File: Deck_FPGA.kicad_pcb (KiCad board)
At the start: 4 copper layers, 41 x 30 mm, 72 parts, among them J1 Left side, J2 Right Side, J3 Conn_01x06, U1 XC7A100T-CSG324, U2 TPS65023BRSBT, U3 S25FL128SAGNFI000, U4 LM3880, X1 ASE-100MHz

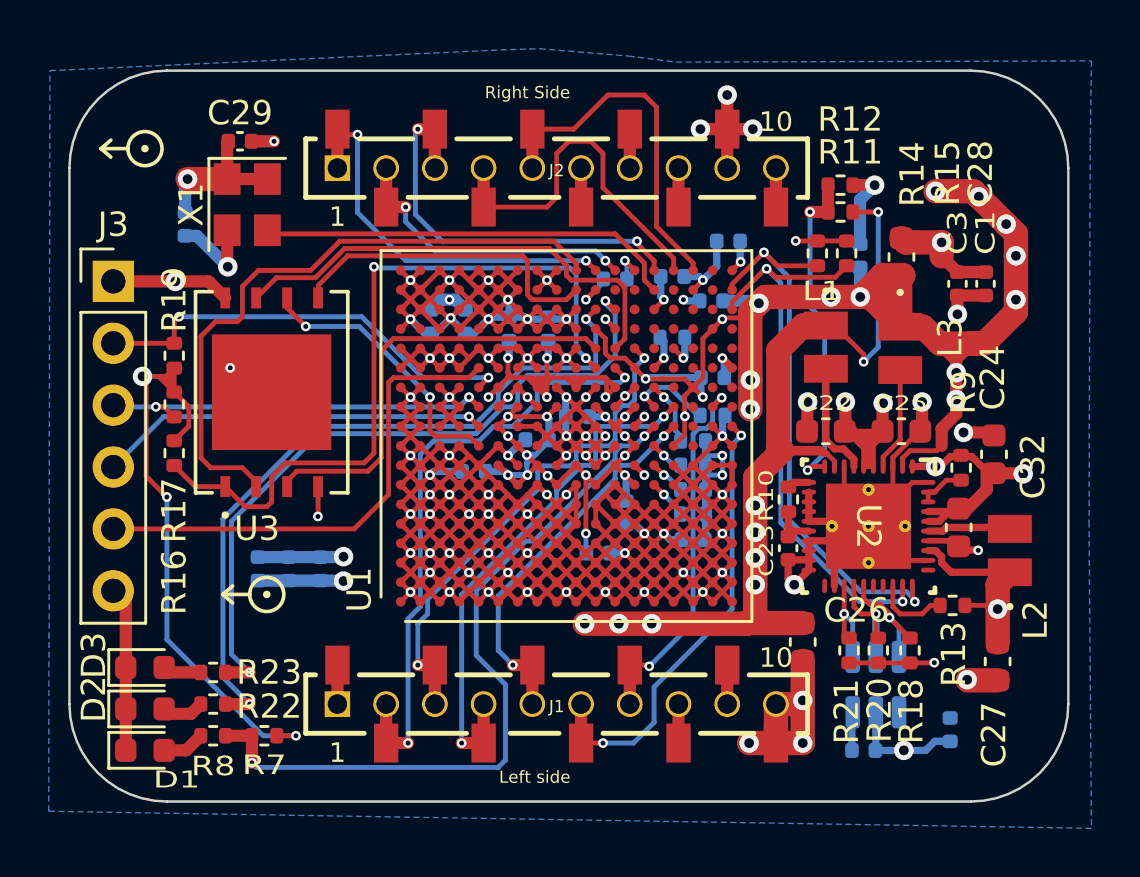
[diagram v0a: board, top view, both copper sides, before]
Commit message: added PowerIC filtering resistor and pull up for SPI Flash SIO2/SIO3
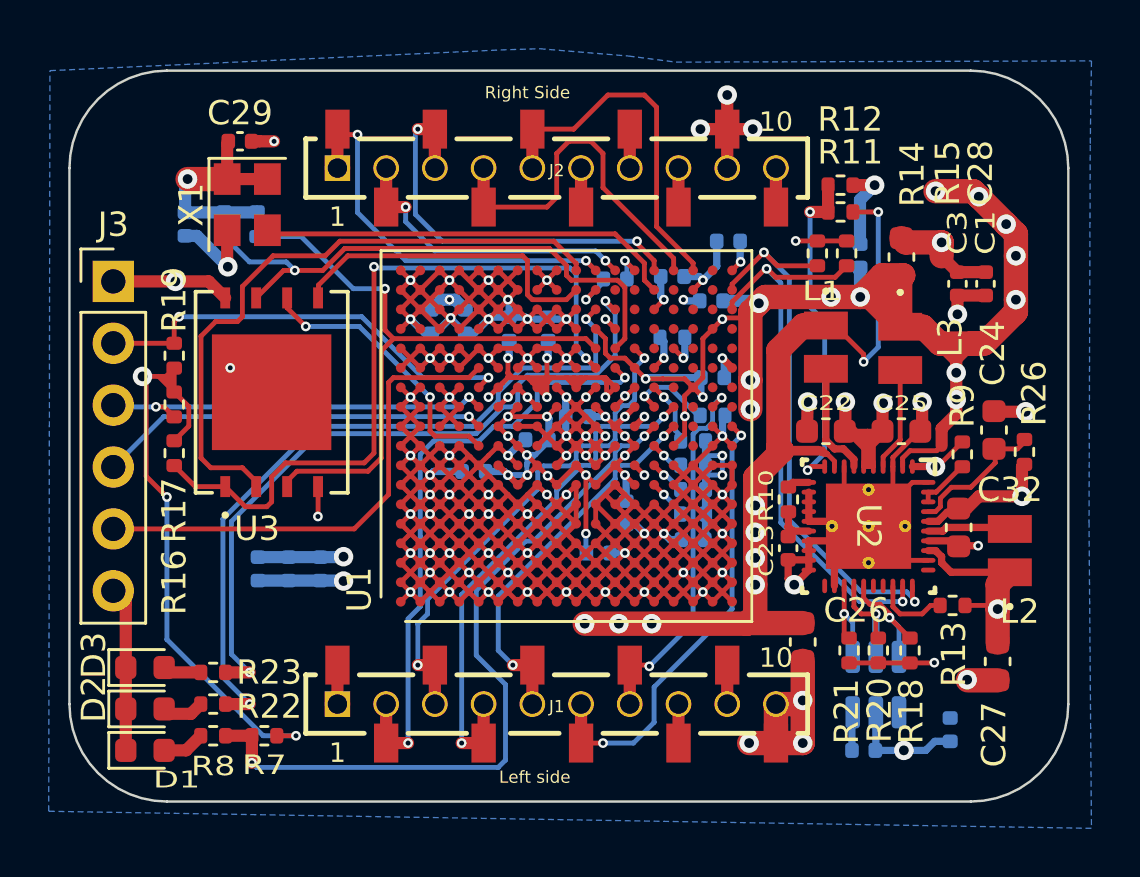
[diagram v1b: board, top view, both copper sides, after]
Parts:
- removed REF** (x2): arrow, ul:arrow
- added R24: 4k7, Resistor_SMD:R_0402_1005Metric, B.Cu at (87.7, 102.3)
- added R25: 4k7, Resistor_SMD:R_0402_1005Metric, B.Cu at (86.3, 102.3)
- added R26: 10R, Resistor_SMD:R_0402_1005Metric, F.Cu at (119.2, 111.7)
- C22, C25, C32: value 10u -> 22u
- R14, R15: value 100k -> 4k7
- moved C24 1.00 mm to (118.0, 110.8)
- moved R9 0.55 mm to (116.7, 111.8)
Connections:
- C24 pad 1: VBUS -> /VCC
- U2 pad 37: VBUS -> /VCC
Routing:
- net /SIO2: track 18.1 -> 26.4 mm, vias 0 -> 1
- net /VCC: track 0.00 -> 5.82 mm
- net /SIO3: track 19.5 -> 23.0 mm, vias 0 -> 1
- net +3V3: track 110.8 -> 113.8 mm
- net VBUS: track 33.4 -> 31.0 mm

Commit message: fixed caps, jlc references
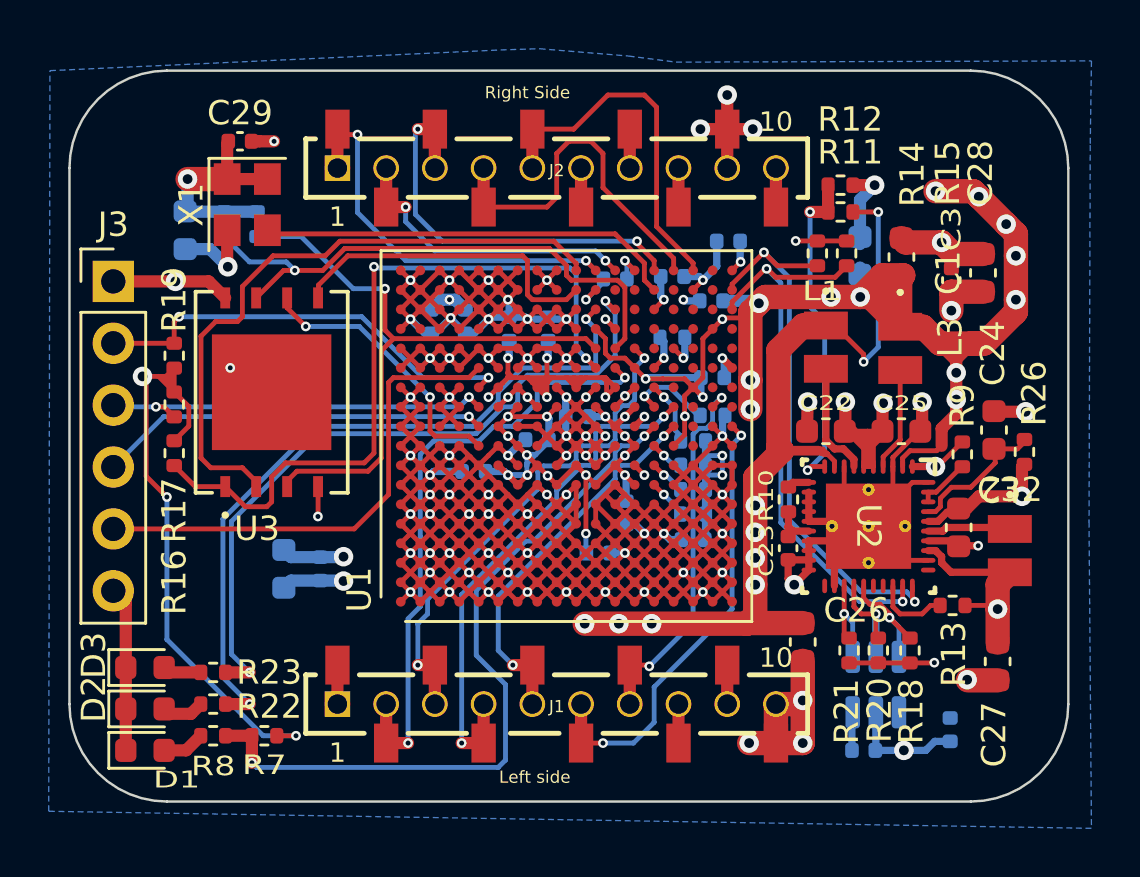
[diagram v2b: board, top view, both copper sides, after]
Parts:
- removed C2: 47u, Capacitor_SMD:C_0402_1005Metric
- C1, C15, C19, C7: footprint Capacitor_SMD:C_0402_1005Metric -> Capacitor_SMD:C_0603_1608Metric
- C29: value 100nF -> 100n
- C30: value 100n -> 470n
- D1: value LED -> LED_RED
- D2: value LED -> LED_BLUE
- D3: value LED -> LED_YELLOW
- R11: value 100K -> 100k
- R12: value 150K -> 150k
- R13: value 10k -> 4k7
- R22, R23, R7: value 200 -> 200R
- R8: value 100 -> 100R
- moved C1 0.46 mm to (117.5, 104.3)
- moved C3 0.29 mm to (116.2, 104.6)
- moved C19 0.25 mm to (84.8, 102.5)
- moved C15 0.20 mm to (88.8, 116.5)
- turned L2 to -90 degrees
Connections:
- L2 pad 1: +1V8 -> /L2
- L2 pad 2: /L2 -> +1V8
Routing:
- net GND: track 440.6 -> 439.3 mm
- net +1V0: track 68.0 -> 67.1 mm
